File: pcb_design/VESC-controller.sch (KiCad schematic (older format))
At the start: 18 parts, among them J1 GATE_DRIVER_CONN_U, J2 GATE_DRIVER_CONN_V, J3 GATE_DRIVER_CONN_W, J4 micro USB, J5 ACCEL, J6 REGEN, J7 12V, J8 V_BUS, P1 HALL/Encoder, P101 CANBUS, P3 PWR_COMM

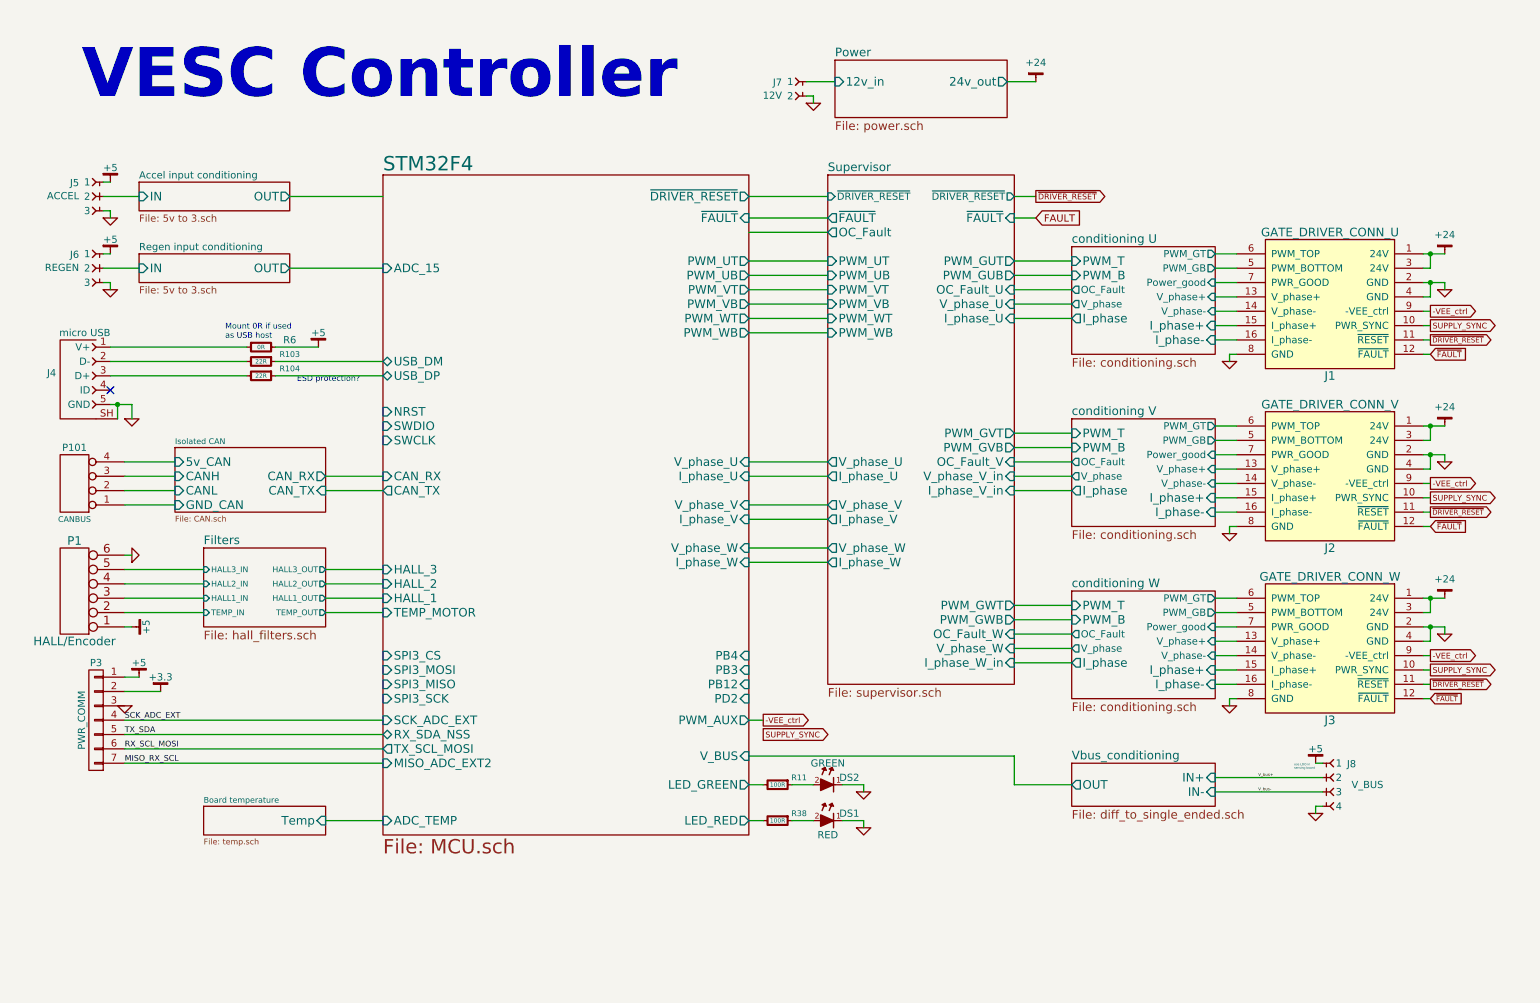
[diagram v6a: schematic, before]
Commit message: Fixed issue with non-bidirectional phase current measurement. Started routing power supplies. Changed terminal blocks from 5.00mm to 3.81mm pitch
Signed-off-by: Marcos Chaparro <mchaparro@paltatech.com>
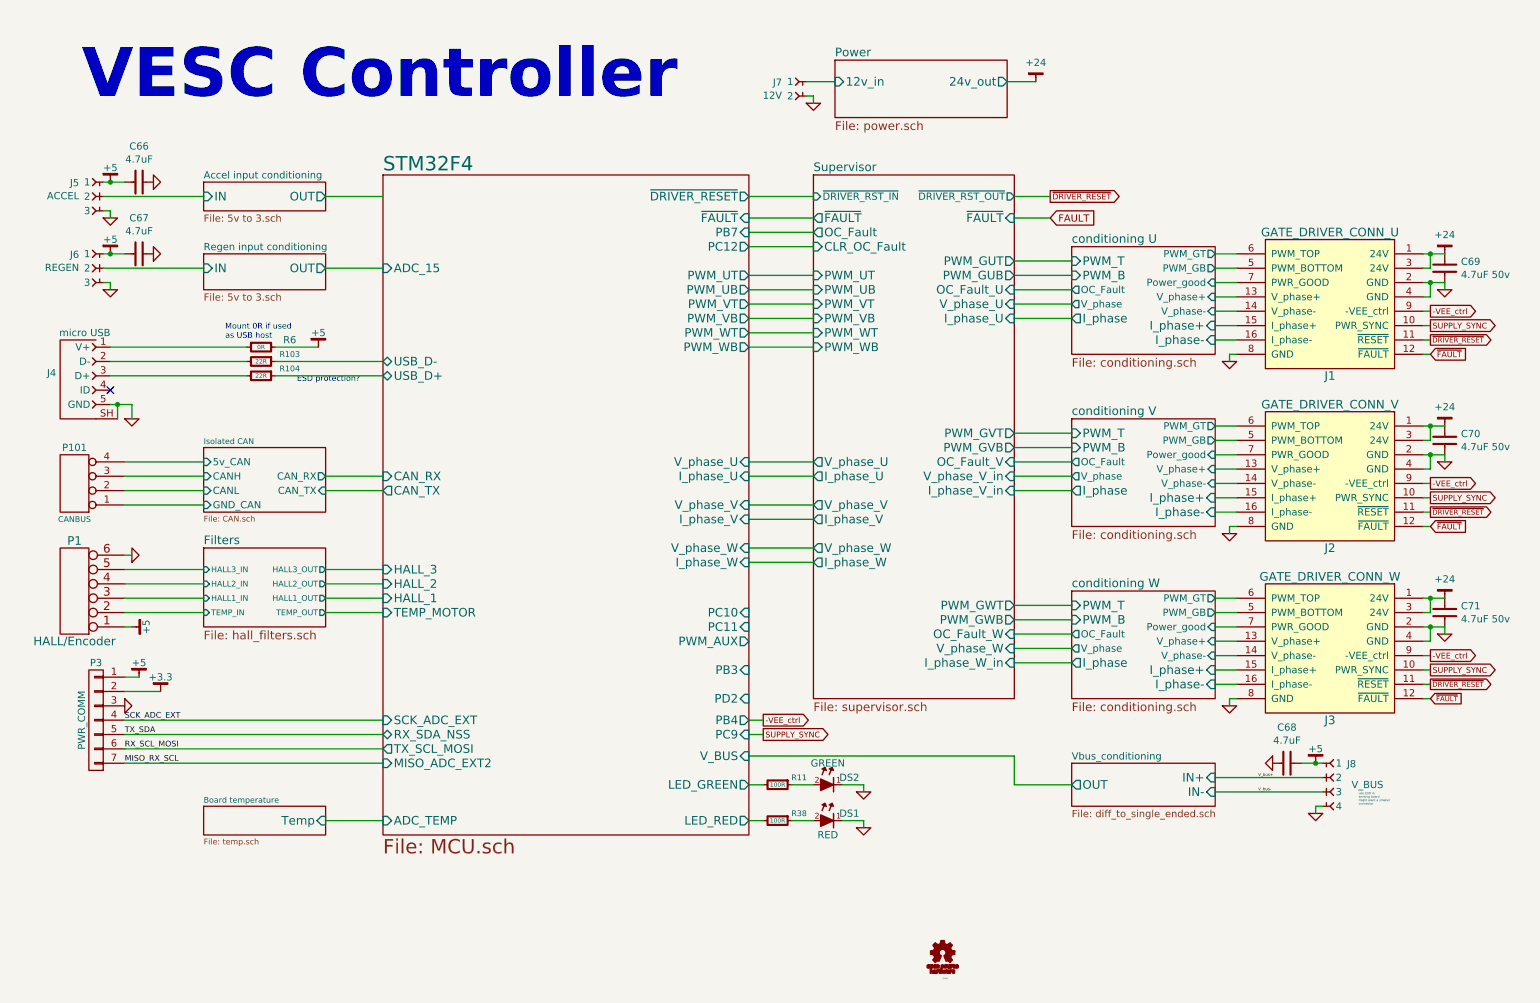
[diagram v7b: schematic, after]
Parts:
- added C66, C67, C68: 4.7uF, IPC7351-Nominal:CAPC2012X70, symbol C-0805
- added C69, C70, C71: 4.7uF 50v, IPC7351-Nominal:CAPC3216X70, symbol C-1206
- added SYM1: OSHW-SCHEM-PCB10mm, mech:OSHW-10mm, symbol OSHW-SCHEM-PCB10mm
- J5, J6: footprint w_conn_mkds:mkds_1,5-2 -> conn-phoenix:mcv_1,5-3-G-3,81
- J7: footprint w_conn_mkds:mkds_1,5-2 -> conn-phoenix:mcv_1,5-2-G-3,81
- J8: footprint w_conn_mkds:mkds_1,5-4 -> conn-phoenix:mcv_1,5-4-G-3,81
- P1: footprint w_conn_mkds:mkds_1,5-6 -> conn-phoenix:mcv_1,5-6-G-3,81
- P3: footprint w_conn_mkds:mkds_1,5-7 -> conn-phoenix:mcv_1,5-7-G-3,81
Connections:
- net +24: now also C69.1, C70.1, C71.1
- net +5: now also C66.2, C67.2, C68.1
- net GND: now also C66.1, C67.1, C68.2, C69.2, C70.2, C71.2
- net STM32F4/USB_DM renamed STM32F4/USB_D-
- net STM32F4/USB_DP renamed STM32F4/USB_D+
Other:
- note added: "use LDO in\nsensing board\nmight want a smaller\nconnector"
- note removed: "use LDO in\nsensing board"

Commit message: More layout
Signed-off-by: Marcos Chaparro <mchaparro@paltatech.com>
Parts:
- added P2: Resolver, conn-phoenix:mcv_1,5-6-G-3,81, symbol CONN_6
- J1, J2, J3: footprint conn-100mil:CONN-100MIL-M-2x7 -> conn-100mil:CONN-100MIL-M-2x8
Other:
- note added: "ESD protection\n"
- note removed: "ESD protection?\n"
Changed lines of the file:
@@
 $EndComp
 $Comp
-L GND-RESCUE-BLDC_4 #PWR01
+L GND-RESCUE-BLDC_4 #PWR7
 U 1 1 522DA053
 P 1500 4400
-F 0 "#PWR01" H 1500 4400 30  0001 C CNN
+F 0 "#PWR7" H 1500 4400 30  0001 C CNN
 F 1 "GND" H 1500 4330 30  0001 C CNN
 F 2 "" H 1500 4400 60  0001 C CNN
@@
 $EndComp
 $Comp
-L GND-RESCUE-BLDC_4 #PWR02
+L GND-RESCUE-BLDC_4 #PWR5
 U 1 1 522DA0E2
 P 1450 5450
-F 0 "#PWR02" H 1450 5450 30  0001 C CNN
+F 0 "#PWR5" H 1450 5450 30  0001 C CNN
 F 1 "GND" H 1450 5380 30  0001 C CNN
 F 2 "" H 1450 5450 60  0001 C CNN
@@
 $EndComp
 $Comp
-L GND-RESCUE-BLDC_4 #PWR03
+L GND-RESCUE-BLDC_4 #PWR6
 U 1 1 522DA0FC
 P 1500 3450
-F 0 "#PWR03" H 1500 3450 30  0001 C CNN
+F 0 "#PWR6" H 1500 3450 30  0001 C CNN
 F 1 "GND" H 1500 3380 30  0001 C CNN
 F 2 "" H 1500 3450 60  0001 C CNN
@@
 Text Notes 2150 2900 0    40   ~ 0
 Mount 0R if used\nas USB host
-Text Notes 2650 3200 0    40   ~ 0
-ESD protection?\n
+Text Notes 2200 3300 0    40   ~ 0
+ESD protection\n
 Text Label 1450 5750 0    40   ~ 0
 RX_SCL_MOSI
@@
 $EndComp
 $Comp
-L GND-RESCUE-BLDC_4 #PWR04
+L GND-RESCUE-BLDC_4 #PWR16
 U 1 1 53FC131A
 P 6600 6300
-F 0 "#PWR04" H 6600 6300 30  0001 C CNN
+F 0 "#PWR16" H 6600 6300 30  0001 C CNN
 F 1 "GND" H 6600 6230 30  0001 C CNN
 F 2 "" H 6600 6300 60  0001 C CNN
@@
 MISO_RX_SCL
 $Comp
-L GND #PWR05
+L GND #PWR25
 U 1 1 58876637
 P 10650 2550
-F 0 "#PWR05" H 10650 2550 30  0001 C CNN
+F 0 "#PWR25" H 10650 2550 30  0001 C CNN
 F 1 "GND" H 10650 2480 30  0001 C CNN
 F 2 "" H 10650 2550 60  0000 C CNN
@@
 ~DRIVER_RESET
 Text GLabel 7900 2050 2    50   Input ~ 0
-FAULT
+~FAULT
 $Sheet
 S 8050 2250 1000 750
@@
 F 0 "J1" H 9850 2150 60  0000 C CNN
 F 1 "GATE_DRIVER_CONN_U" H 9850 3150 60  0000 C CNN
-F 2 "conn-100mil:CONN-100MIL-M-2x7" H 9950 2650 60  0001 C CNN
+F 2 "conn-100mil:CONN-100MIL-M-2x8" H 9950 2650 60  0001 C CNN
 F 3 "" H 9950 2650 60  0001 C CNN
 	1    9850 2650
@@
 	9200 2700 9050 2700
 $Comp
-L GND #PWR06
+L GND #PWR18
 U 1 1 588B9E09
 P 9150 3050
-F 0 "#PWR06" H 9150 3050 30  0001 C CNN
+F 0 "#PWR18" H 9150 3050 30  0001 C CNN
 F 1 "GND" H 9150 2980 30  0001 C CNN
 F 2 "" H 9150 3050 60  0000 C CNN
@@
 	9200 2900 9050 2900
 $Comp
-L GND #PWR07
+L GND #PWR27
 U 1 1 588C277E
 P 10650 3750
-F 0 "#PWR07" H 10650 3750 30  0001 C CNN
+F 0 "#PWR27" H 10650 3750 30  0001 C CNN
 F 1 "GND" H 10650 3680 30  0001 C CNN
 F 2 "" H 10650 3750 60  0000 C CNN
@@
 F 0 "J2" H 9850 3350 60  0000 C CNN
 F 1 "GATE_DRIVER_CONN_V" H 9850 4350 60  0000 C CNN
-F 2 "conn-100mil:CONN-100MIL-M-2x7" H 9950 3850 60  0001 C CNN
+F 2 "conn-100mil:CONN-100MIL-M-2x8" H 9950 3850 60  0001 C CNN
 F 3 "" H 9950 3850 60  0001 C CNN
 	1    9850 3850
@@
 	9200 3900 9050 3900
 $Comp
-L GND #PWR08
+L GND #PWR19
 U 1 1 588C27A8
 P 9150 4250
-F 0 "#PWR08" H 9150 4250 30  0001 C CNN
+F 0 "#PWR19" H 9150 4250 30  0001 C CNN
 F 1 "GND" H 9150 4180 30  0001 C CNN
 F 2 "" H 9150 4250 60  0000 C CNN
@@
 	8050 5150 7650 5150
 $Comp
-L GND #PWR09
+L GND #PWR29
 U 1 1 588C4E72
 P 10650 4950
-F 0 "#PWR09" H 10650 4950 30  0001 C CNN
+F 0 "#PWR29" H 10650 4950 30  0001 C CNN
 F 1 "GND" H 10650 4880 30  0001 C CNN
 F 2 "" H 10650 4950 60  0000 C CNN
@@
 F 0 "J3" H 9850 4550 60  0000 C CNN
 F 1 "GATE_DRIVER_CONN_W" H 9850 5550 60  0000 C CNN
-F 2 "conn-100mil:CONN-100MIL-M-2x7" H 9950 5050 60  0001 C CNN
+F 2 "conn-100mil:CONN-100MIL-M-2x8" H 9950 5050 60  0001 C CNN
 F 3 "" H 9950 5050 60  0001 C CNN
 	1    9850 5050
@@
 	9200 5100 9050 5100
 $Comp
-L GND #PWR010
+L GND #PWR20
 U 1 1 588C4E9E
 P 9150 5450
-F 0 "#PWR010" H 9150 5450 30  0001 C CNN
+F 0 "#PWR20" H 9150 5450 30  0001 C CNN
 F 1 "GND" H 9150 5380 30  0001 C CNN
 F 2 "" H 9150 5450 60  0000 C CNN
@@
 	6600 6250 6450 6250
 $Comp
-L GND-RESCUE-BLDC_4 #PWR011
+L GND-RESCUE-BLDC_4 #PWR15
 U 1 1 588CB158
 P 6600 6050
-F 0 "#PWR011" H 6600 6050 30  0001 C CNN
+F 0 "#PWR15" H 6600 6050 30  0001 C CNN
 F 1 "GND" H 6600 5980 30  0001 C CNN
 F 2 "" H 6600 6050 60  0001 C CNN
@@
 $EndComp
 $Comp
-L GND #PWR012
+L GND #PWR2
 U 1 1 588A7EFE
 P 1350 2050
-F 0 "#PWR012" H 1350 2050 30  0001 C CNN
+F 0 "#PWR2" H 1350 2050 30  0001 C CNN
 F 1 "GND" H 1350 1980 30  0001 C CNN
 F 2 "" H 1350 2050 60  0000 C CNN
@@
 	1350 2500 1350 2550
 $Comp
-L GND #PWR013
+L GND #PWR4
 U 1 1 588A9C10
 P 1350 2550
-F 0 "#PWR013" H 1350 2550 30  0001 C CNN
+F 0 "#PWR4" H 1350 2550 30  0001 C CNN
 F 1 "GND" H 1350 2480 30  0001 C CNN
 F 2 "" H 1350 2550 60  0000 C CNN
@@
 	6400 1100 6200 1100
 $Comp
-L GND #PWR014
+L GND #PWR14
 U 1 1 588CC018
 P 6250 1250
-F 0 "#PWR014" H 6250 1250 30  0001 C CNN
+F 0 "#PWR14" H 6250 1250 30  0001 C CNN
 F 1 "GND" H 6250 1180 30  0001 C CNN
 F 2 "" H 6250 1250 60  0000 C CNN
@@
 	6250 1200 6200 1200
 $Comp
-L +5 #PWR015
+L +5 #PWR1
 U 1 1 588B45C6
 P 1350 1800
-F 0 "#PWR015" H 250 150 30  0001 C CNN
+F 0 "#PWR1" H 250 150 30  0001 C CNN
 F 1 "+5" H 1350 1900 50  0000 C CNN
 F 2 "" H 250 100 60  0000 C CNN
@@
 	1300 1800 1450 1800
 $Comp
-L +5 #PWR016
+L +5 #PWR3
 U 1 1 588B5F6B
 P 1350 2300
-F 0 "#PWR016" H 250 650 30  0001 C CNN
+F 0 "#PWR3" H 250 650 30  0001 C CNN
 F 1 "+5" H 1350 2400 50  0000 C CNN
 F 2 "" H 250 600 60  0000 C CNN
@@
 	1300 2300 1450 2300
 $Comp
-L +5 #PWR017
+L +5 #PWR13
 U 1 1 588BB3A4
 P 2800 2950
-F 0 "#PWR017" H 1700 1300 30  0001 C CNN
+F 0 "#PWR13" H 1700 1300 30  0001 C CNN
 F 1 "+5" H 2800 3050 50  0000 C CNN
 F 2 "" H 1700 1250 60  0000 C CNN
@@
 $EndComp
 $Comp
-L +5 #PWR018
+L +5 #PWR9
 U 1 1 588BE146
 P 1550 5250
-F 0 "#PWR018" H -50 50  30  0001 C CNN
+F 0 "#PWR9" H -50 50  30  0001 C CNN
 F 1 "+5" H 1550 5350 50  0000 C CNN
 F 2 "" H -50 0   60  0000 C CNN
@@
 $EndComp
 $Comp
-L +3.3 #PWR019
+L +3.3 #PWR12
 U 1 1 588BE494
 P 1700 5350
-F 0 "#PWR019" H 50  100 30  0001 C CNN
+F 0 "#PWR12" H 50  100 30  0001 C CNN
 F 1 "+3.3" H 1700 5450 50  0000 C CNN
 F 2 "" H 50  50  60  0000 C CNN
@@
 $EndComp
 $Comp
-L +5 #PWR020
+L +5 #PWR8
 U 1 1 588C053A
 P 1500 4900
-F 0 "#PWR020" H -100 -300 30  0001 C CNN
+F 0 "#PWR8" H -100 -300 30  0001 C CNN
 F 1 "+5" H 1500 5000 50  0000 C CNN
 F 2 "" H -100 -350 60  0000 C CNN
@@
 	1500 4900 1450 4900
 $Comp
-L +24 #PWR021
+L +24 #PWR17
 U 1 1 588CE8C9
 P 7800 1100
-F 0 "#PWR021" H -650 250 30  0001 C CNN
+F 0 "#PWR17" H -650 250 30  0001 C CNN
 F 1 "+24" H 7800 1233 50  0000 C CNN
 F 2 "" H -650 200 60  0000 C CNN
@@
 $EndComp
 $Comp
-L +24 #PWR022
+L +24 #PWR24
 U 1 1 588D0DE1
 P 10650 2300
-F 0 "#PWR022" H 10700 2350 30  0001 C CNN
+F 0 "#PWR24" H 10700 2350 30  0001 C CNN
 F 1 "+24" H 10650 2433 50  0000 C CNN
 F 2 "" H -50 0   60  0000 C CNN
@@
 $EndComp
 $Comp
-L +24 #PWR023
+L +24 #PWR26
 U 1 1 588D1EB4
 P 10650 3500
-F 0 "#PWR023" H 10700 3550 30  0001 C CNN
+F 0 "#PWR26" H 10700 3550 30  0001 C CNN
 F 1 "+24" H 10650 3633 50  0000 C CNN
 F 2 "" H -50 50  60  0000 C CNN
@@
 $EndComp
 $Comp
-L +24 #PWR024
+L +24 #PWR28
 U 1 1 588D2D5A
 P 10650 4700
-F 0 "#PWR024" H 10700 4750 30  0001 C CNN
+F 0 "#PWR28" H 10700 4750 30  0001 C CNN
 F 1 "+24" H 10650 4833 50  0000 C CNN
 F 2 "" H -50 0   60  0000 C CNN
@@
 	9800 6050 9050 6050
 $Comp
-L GND #PWR025
+L GND #PWR23
 U 1 1 588E5603
 P 9750 6200
-F 0 "#PWR025" H 9800 6250 30  0001 C CNN
+F 0 "#PWR23" H 9800 6250 30  0001 C CNN
 F 1 "GND" H 0   30  30  0001 C CNN
 F 2 "" H 0   100 60  0000 C CNN
@@
 	9750 6150 9800 6150
 $Comp
-L +5 #PWR026
+L +5 #PWR22
 U 1 1 588E703F
 P 9750 5850
-F 0 "#PWR026" H 8650 4200 30  0001 C CNN
+F 0 "#PWR22" H 8650 4200 30  0001 C CNN
 F 1 "+5" H 9750 5950 50  0000 C CNN
 F 2 "" H 8650 4150 60  0000 C CNN
@@
 $EndComp
 $Comp
-L GND #PWR027
+L GND #PWR21
 U 1 1 588D02C2
 P 9450 5850
-F 0 "#PWR027" H 9500 5900 30  0001 C CNN
+F 0 "#PWR21" H 9500 5900 30  0001 C CNN
 F 1 "GND" H -300 -320 30  0001 C CNN
 F 2 "" H -300 -250 60  0000 C CNN
@@
 $EndComp
 $Comp
-L GND #PWR028
+L GND #PWR10
 U 1 1 588DFDA4
 P 1650 1800
-F 0 "#PWR028" H 1650 1800 30  0001 C CNN
+F 0 "#PWR10" H 1650 1800 30  0001 C CNN
 F 1 "GND" H 1650 1730 30  0001 C CNN
 F 2 "" H 1650 1800 60  0000 C CNN
@@
 Connection ~ 1350 2300
 $Comp
-L GND #PWR029
+L GND #PWR11
 U 1 1 588E1A2D
 P 1650 2300
-F 0 "#PWR029" H 1650 2300 30  0001 C CNN
+F 0 "#PWR11" H 1650 2300 30  0001 C CNN
 F 1 "GND" H 1650 2230 30  0001 C CNN
 F 2 "" H 1650 2300 60  0000 C CNN
@@
 Wire Wire Line
 	5800 5650 5900 5650
+$Comp
+L CONN_6 P2
+U 1 1 588DDA44
+P 1100 6400
+F 0 "P2" H 1100 6050 60  0000 C CNN
+F 1 "Resolver" H 1100 6750 60  0000 C CNN
+F 2 "conn-phoenix:mcv_1,5-6-G-3,81" H 1100 6400 60  0001 C CNN
+F 3 "" H 1100 6400 60  0001 C CNN
+	1    1100 6400
+	-1   0    0    1
+$EndComp
 $EndSCHEMATC
